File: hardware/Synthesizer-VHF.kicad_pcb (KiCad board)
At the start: 4 copper layers, 38.9 x 37.7 mm, 85 parts, among them J1 Screw_Terminal_01x02, J2 Scope, J4 USB-C 2.0 16P, J5 REF_IN, J6 Scope, J7 RFOUTA, J8 Header 1x3, J9 RFOUTB, U1 LM7805A, U2 FT231XQ, U3 ATtiny1616-M, U4 ADF4351, U7 ADP150AUJZ-3.3-R7, U8 ADP150AUJZ-3.3-R7, X1 HCI 8122S-25NQ33FTL

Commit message: Stitch one floating GND island and keep out two slivers
A 0.45/0.3 mm GND via at (163.177, 100.862) ties the F.Cu island
to the plane. The RF_GCPW_N triangle and RF_GCPW_S fragment are
too narrow for that via, so F.Cu pour keepouts remove them.

Co-authored-by: Jeffrey Millar <wa1hco@users.noreply.github.com>
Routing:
- net GND: vias 185 -> 186
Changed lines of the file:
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@@
 	)
 	(via
+		(at 163.177 100.862)
+		(size 0.45)
+		(drill 0.3)
+		(layers "F.Cu" "B.Cu")
+		(free yes)
+		(net "GND")
+	)
+	(via
 		(at 140.824967 95.406304)
 		(size 0.45)
@@
 	)
 	(zone
+		(layer "F.Cu")
+		(name "float_gnd_s")
+		(hatch edge 0.5)
+		(connect_pads
+			(clearance 0)
+		)
+		(min_thickness 0.25)
+		(keepout
+			(tracks allowed)
+			(vias allowed)
+			(pads allowed)
+			(copperpour not_allowed)
+			(footprints allowed)
+		)
+		(placement
+			(enabled no)
+			(sheetname "")
+		)
+		(fill
+			(thermal_gap 0.5)
+			(thermal_bridge_width 0.5)
+			(island_removal_mode 0)
+		)
+		(polygon
+			(pts
+				(xy 163.029783 101.09) (xy 163.279 101.09) (xy 163.279 101.14) (xy 163.340218 101.14) (xy 163.352046 101.12)
+				(xy 163.469107 101.12) (xy 163.469107 102.126744) (xy 163.424751 102.082388) (xy 163.387981 102.015049)
+				(xy 163.384607 101.98367) (xy 163.384607 101.67298) (xy 163.384608 101.672967) (xy 163.384608 101.580672)
+				(xy 163.363789 101.502977) (xy 163.344576 101.469699) (xy 163.323567 101.43331) (xy 163.263617 101.37336)
+				(xy 163.263616 101.37336) (xy 163.147369 101.257112) (xy 163.112538 101.237002) (xy 163.077708 101.216892)
+				(xy 163.072989 101.215628) (xy 163.060201 101.207832) (xy 163.04267 101.20388) (xy 163.026063 101.18702)
+				(xy 163.007091 101.175454) (xy 163.000023 101.16483) (xy 162.989728 101.150128) (xy 162.985408 101.145743)
+				(xy 162.985107 101.144318) (xy 162.910789 101.07) (xy 163.009783 101.07)
+			)
+		)
+	)
+	(zone
 		(net "GND")
 		(layer "F.Cu")
@@
 			)
 		)
+	)
+	(zone
+		(layer "F.Cu")
+		(name "float_gnd_n")
+		(hatch edge 0.5)
+		(connect_pads
+			(clearance 0)
+		)
+		(min_thickness 0.25)
+		(keepout
+			(tracks allowed)
+			(vias allowed)
+			(pads allowed)
+			(copperpour not_allowed)
+			(footprints allowed)
+		)
+		(placement
+			(enabled no)
+			(sheetname "")
+		)
+		(fill
+			(thermal_gap 0.5)
+			(thermal_bridge_width 0.5)
+			(island_removal_mode 0)
+		)
+		(polygon
+			(pts
+				(xy 161.632 82.16388) (xy 161.269694 81.801574) (xy 161.632 81.439268)
+			)
+		)

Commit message: Grow the board outline to 45 x 64 mm
Center the existing layout east-west in an extruded-enclosure outline
and add the extra length mostly on the north. Extend the GND and VCC
pours to the new edge and update the Dwgs.User dimensions.

Co-authored-by: Jeffrey Millar <wa1hco@users.noreply.github.com>
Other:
- board size 38.9 x 37.7 mm -> 45 x 64 mm
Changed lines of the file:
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@@
 	)
 	(gr_rect
-		(start 134.55 76)
-		(end 173.5 113.7)
+		(start 131.525 53.7)
+		(end 176.525 117.7)
 		(stroke
 			(width 0.05)
@@
 		(layer "Dwgs.User")
 		(pts
-			(xy 134.55 113.7) (xy 168.6 113.7)
+			(xy 131.525 117.7) (xy 168.6 117.7)
 		)
 		(height 14.15)
@@
 			(keep_text_aligned yes)
 		)
-		(gr_text "34.05 mm"
-			(at 151.9 129.65 0)
+		(gr_text "37.08 mm"
+			(at 150.0625 133.65 0)
 			(layer "Dwgs.User")
 			(effects
@@
 		(layer "Dwgs.User")
 		(pts
-			(xy 153.7 113.7) (xy 168.6 113.7)
+			(xy 153.7 117.7) (xy 168.6 117.7)
 		)
 		(height 9.95)
@@
 		)
 		(gr_text "14.90 mm"
-			(at 161.4 125.05 0)
+			(at 161.4 129.05 0)
 			(layer "Dwgs.User")
 			(effects
@@
 		(layer "Dwgs.User")
 		(pts
-			(xy 134.55 76) (xy 168 76)
+			(xy 131.525 53.7) (xy 168 53.7)
 		)
 		(height -9.15)
@@
 			(keep_text_aligned yes)
 		)
-		(gr_text "33.45 mm"
-			(at 153.75 65.4 0)
+		(gr_text "36.48 mm"
+			(at 153.75 43.1 0)
 			(layer "Dwgs.User")
 			(effects
@@
 		(layer "Dwgs.User")
 		(pts
-			(xy 134.55 75.95) (xy 173.5 75.95)
+			(xy 131.525 53.65) (xy 176.525 53.65)
 		)
 		(height -12.7)
@@
 			(keep_text_aligned yes)
 		)
-		(gr_text "38.95 mm"
-			(at 153.8 61.75 0)
+		(gr_text "45.00 mm"
+			(at 154.025 39.45 0)
 			(layer "Dwgs.User")
 			(effects
@@
 		(layer "Dwgs.User")
 		(pts
-			(xy 134.55 76) (xy 134.55 113.7)
+			(xy 131.525 53.7) (xy 131.525 117.7)
 		)
 		(height 2.65)
@@
 			(keep_text_aligned yes)
 		)
-		(gr_text "37.70 mm"
-			(at 130.1 94.85 90)
+		(gr_text "64.00 mm"
+			(at 127.075 85.7 90)
 			(layer "Dwgs.User")
 			(effects
@@
 		(layer "Dwgs.User")
 		(pts
-			(xy 134.55 113.7) (xy 153.7 113.7)
+			(xy 131.525 117.7) (xy 153.7 117.7)
 		)
 		(height 9.95)
@@
 			(keep_text_aligned yes)
 		)
-		(gr_text "19.15 mm"
-			(at 144.2 125.1 0)
+		(gr_text "22.18 mm"
+			(at 142.6125 129.1 0)
 			(layer "Dwgs.User")
 			(effects
@@
 		(polygon
 			(pts
-				(xy 173.5 76) (xy 134.55 76) (xy 134.55 113.7) (xy 173.5 113.7)
+				(xy 176.525 53.7) (xy 131.525 53.7) (xy 131.525 117.7) (xy 176.525 117.7)
 			)
 		)
@@
 		(polygon
 			(pts
-				(xy 173.5 76) (xy 134.55 76) (xy 134.55 113.7) (xy 173.5 113.7)
+				(xy 176.525 53.7) (xy 131.525 53.7) (xy 131.525 117.7) (xy 176.525 117.7)
 			)
 		)
@@
 		(polygon
 			(pts
-				(xy 173.5 76) (xy 134.55 76) (xy 134.55 113.7) (xy 173.5 113.7)
+				(xy 176.525 53.7) (xy 131.525 53.7) (xy 131.525 117.7) (xy 176.525 117.7)
 			)
 		)
@@
 		(polygon
 			(pts
-				(xy 173.5 76) (xy 134.55 76) (xy 134.55 113.7) (xy 173.5 113.7)
+				(xy 176.525 53.7) (xy 131.525 53.7) (xy 131.525 117.7) (xy 176.525 117.7)
 			)
 		)

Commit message: Swap J5, J7, and J9 to the Cinch edge-launch SMA
Add a 142-0701-801 land pattern for a 1.57 mm board and place it on
the three connectors without moving them or touching the traces.

Co-authored-by: Jeffrey Millar <wa1hco@users.noreply.github.com>
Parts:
- J5, J7, J9: footprint Synthesizer:SMA_Amphenol_901-143_Horizontal -> Synthesizer:SMA_Cinch_142-0701-801_EdgeMount

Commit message: WIP: user edits (connector placement)
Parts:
- moved J5 23.7 mm to (167.8, 56.8)
- moved J4 23.5 mm to (137.5, 56.6)
- moved R12 23.5 mm to (133.8, 74.1)
- moved R13 23.5 mm to (138.1, 66.9)
- moved R24 23.5 mm to (136.9, 66.9)
- moved C7 23.5 mm to (135.4, 67.9)
- moved R16 23.5 mm to (134.7, 75.1)
- moved R8 23.5 mm to (133.2, 71.6)
- moved C2 23.5 mm to (143.0, 63.9)
- moved D6 23.5 mm to (138.8, 63.9)
- moved R1 23.5 mm to (134.5, 62.4)
- moved R3 23.5 mm to (139.4, 62.4)
- moved D2 23.5 mm to (136.1, 63.9)
- moved C1 23.5 mm to (142.9, 82.0)
- moved C9 23.5 mm to (136.4, 65.2)
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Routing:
- net Net-(J5-In): track 4.97 -> 27.2 mm
- net Net-(J7-In): track 11.0 -> 1.77 mm
- net Net-(J9-In): track 10.9 -> 2.31 mm
- net /RXD_U: track 4.44 -> 1.55 mm
- net /5V: track 98.3 -> 97.7 mm
- net /UPDI: track 29.1 -> 28.5 mm
- net GND: track 61.1 -> 60.6 mm, vias 186 -> 143

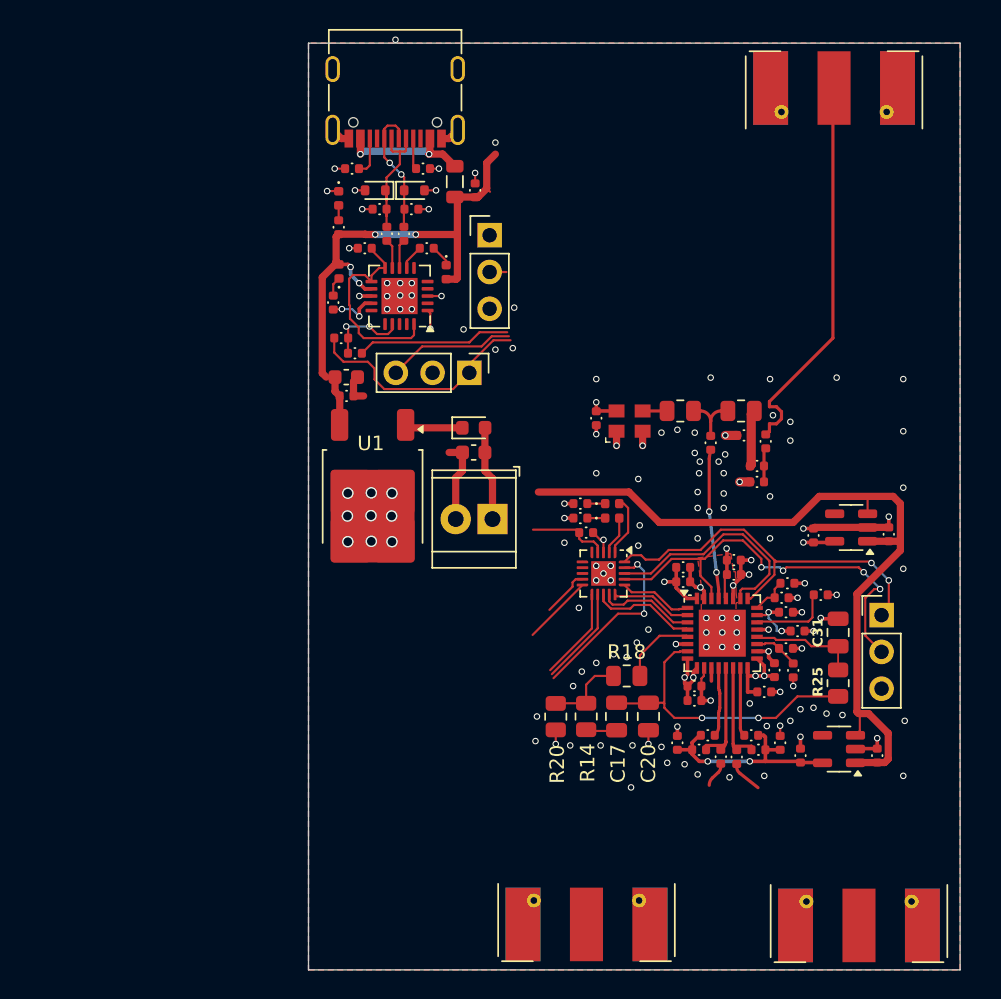
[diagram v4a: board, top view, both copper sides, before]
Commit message: Extruded enclosure WIP: board edits, rules, footprints (USB-C, SMA), Wurth 20x20 shield footprint, upload port
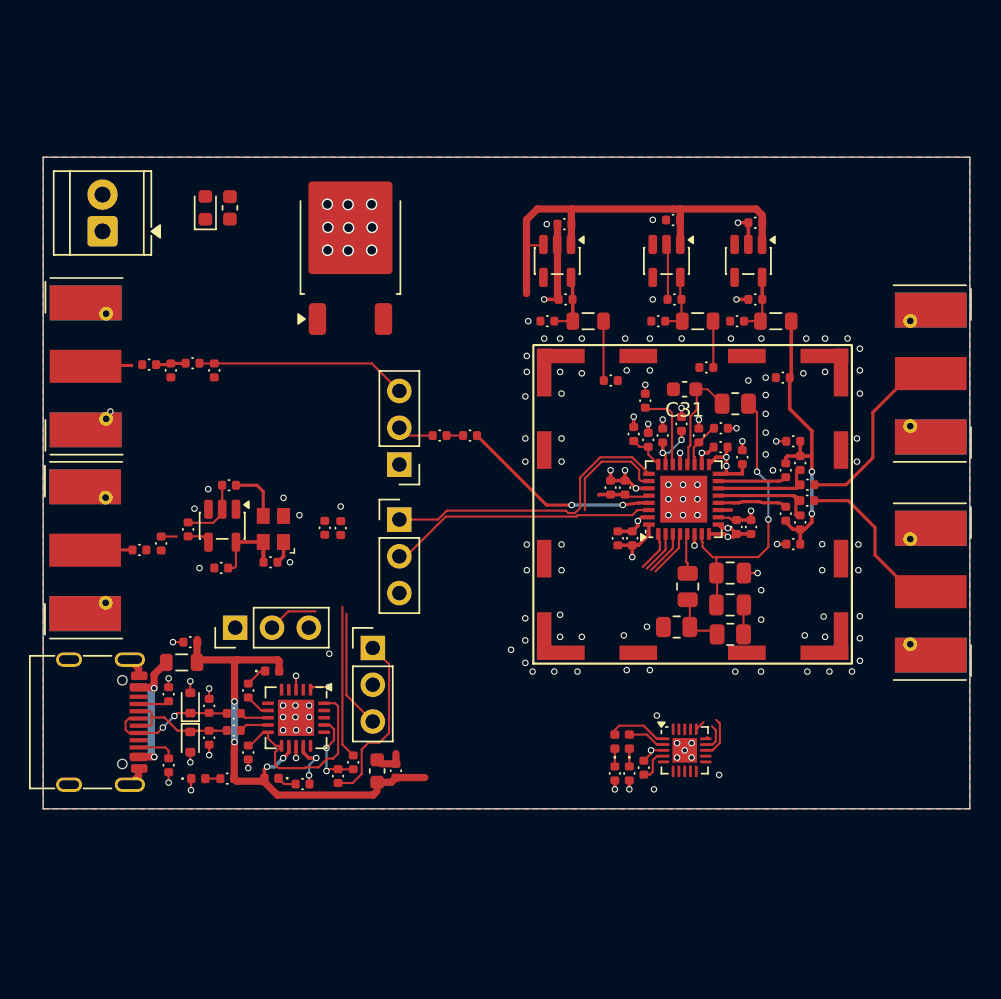
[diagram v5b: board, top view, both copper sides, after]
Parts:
- removed R2: 0R, Resistor_SMD:R_0805_2012Metric
- removed R26: NP, Resistor_SMD:R_0805_2012Metric
- removed U8: ADP150AUJZ-3.3-R7, Package_TO_SOT_SMD:SOT-23-5
- added C34: 10n, Synthesizer:Cap_0402, F.Cu at (119.8, 88.7)
- added C35: 1u 10V, Synthesizer:Cap_0402, F.Cu at (156.7, 65.9)
- added C39: 1u 10V, Synthesizer:Cap_0402, F.Cu at (156.8, 71.4)
- added C40: 100n, Synthesizer:Cap_0402, F.Cu at (126.0, 84.2)
- added C41: 100n, Synthesizer:Cap_0402, F.Cu at (125.5, 89.9)
- added C42: 100p, Synthesizer:Cap_0402, F.Cu at (161.1, 72.9)
- added C43: 100p, Synthesizer:Cap_0402, F.Cu at (164.3, 76.8)
- added C44: 100p, Synthesizer:Cap_0402, F.Cu at (155.7, 72.9)
- added C45: 100p, Synthesizer:Cap_0402, F.Cu at (159.0, 76.1)
- added C46: 100p, Synthesizer:Cap_0402, F.Cu at (148.0, 72.9)
- added C47: 100p, Synthesizer:Cap_0402, F.Cu at (152.4, 77.0)
- added FB2: FerriteBead_Small, Inductor_SMD:L_0805_2012Metric, F.Cu at (163.8, 72.9)
- added FB4: FerriteBead_Small, Inductor_SMD:L_0805_2012Metric, F.Cu at (158.4, 72.9)
- added FB6: FerriteBead_Small, Inductor_SMD:L_0805_2012Metric, F.Cu at (150.8, 72.9)
- added J10: REF_OUT, Synthesizer:SMA_Cinch_142-0701-801_EdgeMount, F.Cu at (115.9, 88.7)
- added J11: Header 1x3, Connector_PinHeader_2.54mm:PinHeader_1x03_P2.54mm_Vertical, F.Cu at (137.8, 82.8)
- added J3: RFShield_TwoPieces, wa1hco:Wurth_WE-SHC_36103205_20x20mm, F.Cu at (158.1, 85.5)
- added R28: 1M, Synthesizer:Res_0402, F.Cu at (123.2, 87.3)
- added R29: 47R, Synthesizer:Res_0402, F.Cu at (121.3, 88.2)
- added R30: 220R, Synthesizer:Res_0402, F.Cu at (132.7, 87.2)
- added R31: 510R, Synthesizer:Res_0402, F.Cu at (133.7, 87.2)
- added R32: 47R, Synthesizer:Res_0402, F.Cu at (140.6, 80.8)
- added U11: SN74LVC1GU04DBVR, Package_TO_SOT_SMD:SOT-23-5, F.Cu at (125.6, 87.0)
- added U5: LP5907MFX-3.3, Package_TO_SOT_SMD:SOT-23-5, F.Cu at (161.9, 68.7)
- added U6: LP5907MFX-3.3, Package_TO_SOT_SMD:SOT-23-5, F.Cu at (156.2, 68.7)
- C31: footprint Capacitor_SMD:C_0805_2012Metric -> Capacitor_SMD:C_0603_1608Metric
- U7: value ADP150AUJZ-3.3-R7 -> LP5907MFX-3.3
- moved J5 55.4 mm to (115.9, 76.0), turned to 90 degrees
- moved J4 49.0 mm to (116.1, 100.6), turned to -90 degrees
- moved R1 43.1 mm to (121.9, 103.6), turned to 90 degrees
- moved C4 42.9 mm to (120.5, 75.9), turned to 180 degrees
- moved D3 41.2 mm to (123.9, 104.5), turned to 0 degrees
- moved R5 41.2 mm to (122.0, 76.3), turned to -90 degrees
- moved R3 40.3 mm to (121.9, 98.7), turned to -90 degrees
- moved D2 40.2 mm to (123.4, 102.0), turned to -90 degrees
- moved R7 39.6 mm to (123.5, 75.8), turned to 0 degrees
- moved R9 38.8 mm to (125.9, 104.5), turned to 0 degrees
- moved D6 38.6 mm to (123.4, 99.3), turned to 90 degrees
- moved J9 38.5 mm to (174.7, 76.5), turned to -90 degrees
- moved C9 38.4 mm to (124.7, 101.7), turned to -90 degrees
- moved FB1 38.2 mm to (122.8, 96.5), turned to 0 degrees
- moved C33 37.8 mm to (162.4, 66.1), turned to 180 degrees
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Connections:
- net Net-(R26-Pad2) renamed /REF_IN
- C13 pad 1: /VCC_1 -> Net-(U4-DVDD)
- C14 pad 1: /VCC_2 -> Net-(U5-OUT)
- C15 pad 1: /VCC_2 -> /VRF
- C18 pad 1: /VCC_1 -> /VVCO
- C19 pad 2: /VCC_1 -> Net-(U4-DVDD)
- C21 pad 2: /VCC_1 -> Net-(U4-DVDD)
- C22 pad 1: /VCC_2 -> /VRF
- C24 pad 1: /VCC_1 -> /VDD
- C25 pad 1: /VCC_1 -> /VDD
- C27 pad 1: /VCC_1 -> Net-(U7-OUT)
- C28 pad 2: /VCC_1 -> /VVCO
- C3 pad 2: Net-(C3-Pad2) -> /REFIN_SEL
- C30 pad 1: /VCC_1 -> Net-(U4-DVDD)
- R11 pad 2: /VCC_2 -> /VRF
- R15 pad 2: /VCC_2 -> /VRF
- R21 pad 2: /VCC_2 -> /VRF
- R23 pad 2: /VCC_2 -> /VRF
- U4 pad 10: /VCC_1 -> /VDD
- U4 pad 16: /VCC_1 -> /VVCO
- U4 pad 17: /VCC_1 -> /VVCO
- U4 pad 28: /VCC_1 -> Net-(U4-DVDD)
- U4 pad 32: /VCC_1 -> Net-(U4-DVDD)
- U4 pad 6: /VCC_1 -> /VDD
- U7 pad 5: /VCC_1 -> Net-(U7-OUT)
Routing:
- net /5V: track 97.7 -> 66.5 mm
- net Net-(J5-In): track 27.2 -> 3.45 mm
- net /VRF: track 0.00 -> 21.1 mm, vias 0 -> 2
- net /UPDI: track 28.5 -> 12.3 mm, vias 2 -> 0
- net /VCC_2: track 15.1 -> 0.00 mm, vias 2 -> 0
- net /VCC_1: track 20.8 -> 6.81 mm, vias 8 -> 0
- net Net-(J9-In): track 2.31 -> 13.1 mm
- net /REF_IN: track 3.92 -> 14.6 mm
- net /MUX: track 29.3 -> 19.1 mm, vias 4 -> 0
- net Net-(J7-In): track 1.77 -> 11.8 mm
- net /VVCO: track 0.00 -> 8.42 mm, vias 0 -> 2
- net /RF_EN: track 15.8 -> 8.04 mm
- net Net-(U4-DVDD): track 0.00 -> 7.52 mm, vias 0 -> 1
- net /TXD_M: track 15.7 -> 8.20 mm
- net /VDD: track 0.00 -> 7.44 mm, vias 0 -> 2
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- added copper zone on In2.Cu, net GND
- removed copper zone on In2.Cu, net /VCC_1
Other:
- board size 45 x 64 mm -> 64 x 45 mm
